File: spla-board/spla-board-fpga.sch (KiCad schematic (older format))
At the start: 4 parts, among them J2 J_JTAG, U1 LFE5U-45F-BG256

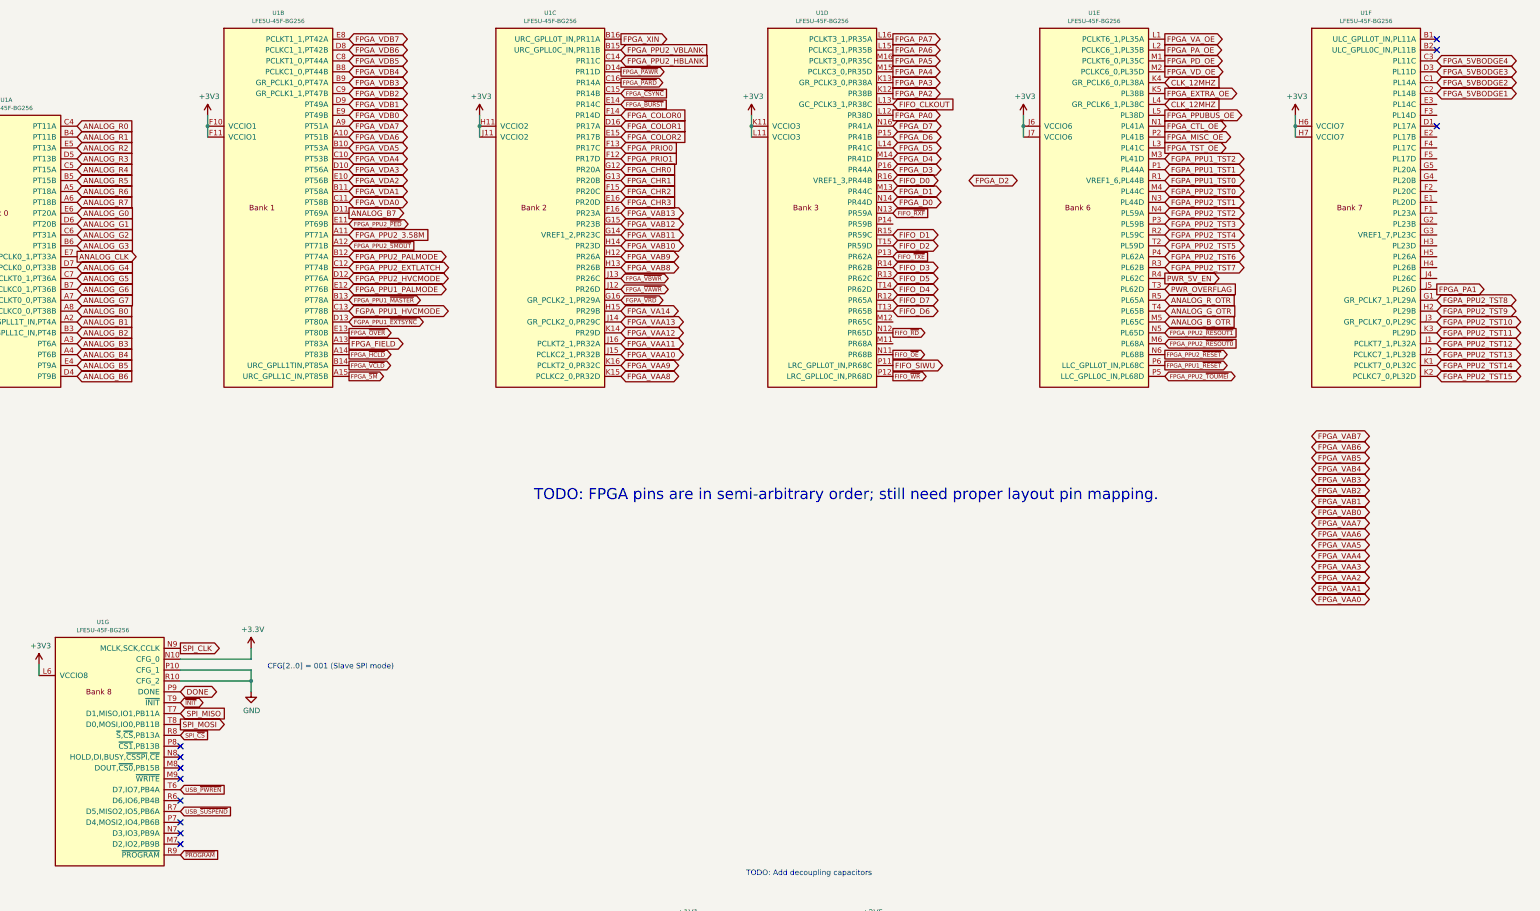
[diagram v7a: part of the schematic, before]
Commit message: schematic: Disconnect FPGA pins temporarily, for pinmapping.
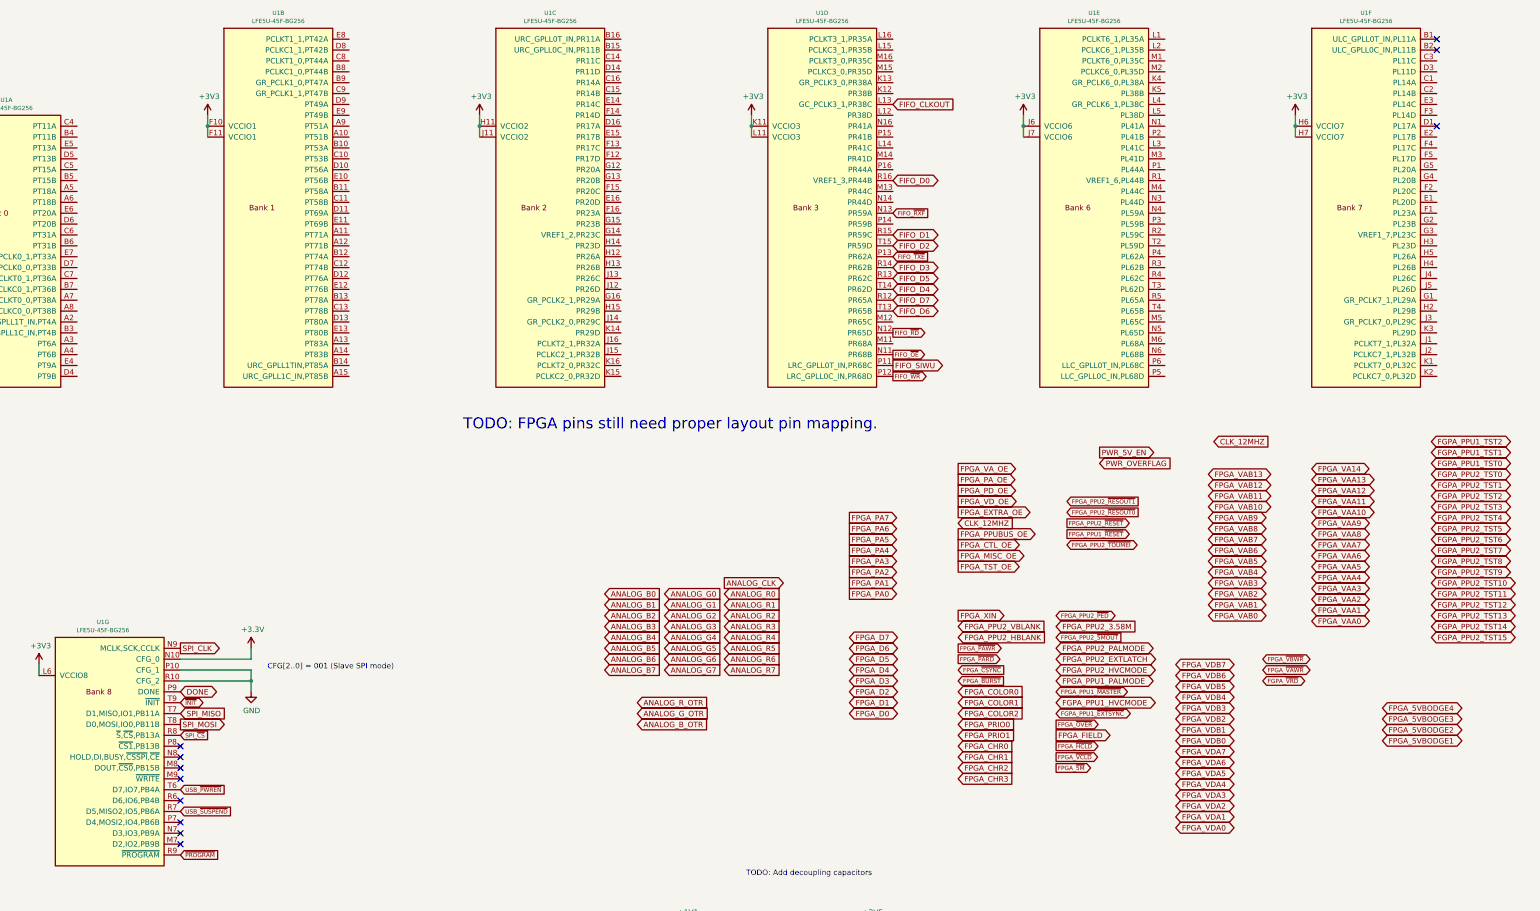
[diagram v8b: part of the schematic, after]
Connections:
- net ANALOG_B0: no longer U1.A8 (PCLKC0_0,PT38B)
- net ANALOG_B1: no longer U1.A2 (ULC_GPLL1T_IN,PT4A)
- net ANALOG_B2: no longer U1.B3 (ULC_GPLL1C_IN,PT4B)
- net ANALOG_B3: no longer U1.A3 (PT6A)
- net ANALOG_B4: no longer U1.A4 (PT6B)
- net ANALOG_B5: no longer U1.E4 (PT9A)
- net ANALOG_B6: no longer U1.D4 (PT9B)
- net ANALOG_B7: no longer U1.D11 (PT69A)
- net ANALOG_B_OTR: no longer U1.M5 (PL65C)
- net ANALOG_CLK: no longer U1.E7 (GR_PCLK0_1,PT33A)
- net ANALOG_G0: no longer U1.E6 (PT20A)
- net ANALOG_G1: no longer U1.D6 (PT20B)
- net ANALOG_G2: no longer U1.C6 (PT31A)
- net ANALOG_G3: no longer U1.B6 (PT31B)
- net ANALOG_G4: no longer U1.D7 (GR_PCLK0_0,PT33B)
- net ANALOG_G5: no longer U1.C7 (PCLKT0_1,PT36A)
- net ANALOG_G6: no longer U1.B7 (PCLKC0_1,PT36B)
- net ANALOG_G7: no longer U1.A7 (PCLKT0_0,PT38A)
- net ANALOG_G_OTR: no longer U1.T4 (PL65B)
- net ANALOG_R0: no longer U1.C4 (PT11A)
- net ANALOG_R1: no longer U1.B4 (PT11B)
- net ANALOG_R2: no longer U1.E5 (PT13A)
- net ANALOG_R3: no longer U1.D5 (PT13B)
- net ANALOG_R4: no longer U1.C5 (PT15A)
- net ANALOG_R5: no longer U1.B5 (PT15B)
- net ANALOG_R6: no longer U1.A5 (PT18A)
- net ANALOG_R7: no longer U1.A6 (PT18B)
- net ANALOG_R_OTR: no longer U1.R5 (PL65A)
- net CLK_12MHZ: no longer U1.K4 (GR_PCLK6_0,PL38A), U1.L4 (GR_PCLK6_1,PL38C)
- net FGPA_PPU1_HVCMODE: no longer U1.C13 (PT78B)
- net FGPA_PPU1_TST0: no longer U1.R1 (VREF1_6,PL44B)
- net FGPA_PPU1_TST1: no longer U1.P1 (PL44A)
- net FGPA_PPU1_TST2: no longer U1.M3 (PL41D)
- net FGPA_PPU1_~EXTSYNC~: no longer U1.D13 (PT80A)
- net FGPA_PPU2_TST0: no longer U1.M4 (PL44C)
- net FGPA_PPU2_TST1: no longer U1.N3 (PL44D)
- net FGPA_PPU2_TST10: no longer U1.J3 (GR_PCLK7_0,PL29C)
- net FGPA_PPU2_TST11: no longer U1.K3 (PL29D)
- net FGPA_PPU2_TST12: no longer U1.J1 (PCLKT7_1,PL32A)
- net FGPA_PPU2_TST13: no longer U1.J2 (PCLKC7_1,PL32B)
- net FGPA_PPU2_TST14: no longer U1.K1 (PCLKT7_0,PL32C)
- net FGPA_PPU2_TST15: no longer U1.K2 (PCLKC7_0,PL32D)
- net FGPA_PPU2_TST2: no longer U1.N4 (PL59A)
- net FGPA_PPU2_TST3: no longer U1.P3 (PL59B)
- net FGPA_PPU2_TST4: no longer U1.R2 (PL59C)
- net FGPA_PPU2_TST5: no longer U1.T2 (PL59D)
- net FGPA_PPU2_TST6: no longer U1.P4 (PL62A)
- net FGPA_PPU2_TST7: no longer U1.R3 (PL62B)
- net FGPA_PPU2_TST8: no longer U1.G1 (GR_PCLK7_1,PL29A)
- net FGPA_PPU2_TST9: no longer U1.H2 (PL29B)
- net FGPA_~VRD~: no longer U1.G16 (GR_PCLK2_1,PR29A)
- net FPGA_5VBODGE1: no longer U1.C2 (PL14B)
- net FPGA_5VBODGE2: no longer U1.C1 (PL14A)
- net FPGA_5VBODGE3: no longer U1.D3 (PL11D)
- net FPGA_5VBODGE4: no longer U1.C3 (PL11C)
- net FPGA_CHR0: no longer U1.G12 (PR20A)
- net FPGA_CHR1: no longer U1.G13 (PR20B)
- net FPGA_CHR2: no longer U1.F15 (PR20C)
- net FPGA_CHR3: no longer U1.E16 (PR20D)
- net FPGA_COLOR0: no longer U1.F14 (PR14D)
- net FPGA_COLOR1: no longer U1.D16 (PR17A)
- net FPGA_COLOR2: no longer U1.E15 (PR17B)
- net FPGA_CTL_OE: no longer U1.N1 (PL41A)
- net FPGA_D0: no longer U1.N14 (PR44D)
- net FPGA_D1: no longer U1.M13 (PR44C)
- net FPGA_D3: no longer U1.P16 (PR44A)
- net FPGA_D4: no longer U1.M14 (PR41D)
- net FPGA_D5: no longer U1.L14 (PR41C)
- net FPGA_D6: no longer U1.P15 (PR41B)
- net FPGA_D7: no longer U1.N16 (PR41A)
- net FPGA_EXTRA_OE: no longer U1.K5 (PL38B)
- net FPGA_FIELD: no longer U1.A13 (PT83A)
- net FPGA_MISC_OE: no longer U1.P2 (PL41B)
- net FPGA_PA0: no longer U1.L12 (PR38D)
- net FPGA_PA1: no longer U1.J5 (PL26D)
- net FPGA_PA2: no longer U1.K12 (PR38B)
- net FPGA_PA3: no longer U1.K13 (GR_PCLK3_0,PR38A)
- net FPGA_PA4: no longer U1.M15 (PCLKC3_0,PR35D)
- net FPGA_PA5: no longer U1.M16 (PCLKT3_0,PR35C)
- net FPGA_PA6: no longer U1.L15 (PCLKC3_1,PR35B)
- net FPGA_PA7: no longer U1.L16 (PCLKT3_1,PR35A)
- net FPGA_PA_OE: no longer U1.L2 (PCLKC6_1,PL35B)
- net FPGA_PD_OE: no longer U1.M1 (PCLKT6_0,PL35C)
- net FPGA_PPU1_PALMODE: no longer U1.E12 (PT76B)
- net FPGA_PPU1_~MASTER~: no longer U1.B13 (PT78A)
- net FPGA_PPU1_~RESET~: no longer U1.P6 (LLC_GPLL0T_IN,PL68C)
- net FPGA_PPU2_3.58M: no longer U1.A11 (PT71A)
- net FPGA_PPU2_EXTLATCH: no longer U1.C12 (PT74B)
- net FPGA_PPU2_HBLANK: no longer U1.C14 (PR11C)
- net FPGA_PPU2_HVCMODE: no longer U1.D12 (PT76A)
- net FPGA_PPU2_PALMODE: no longer U1.B12 (PT74A)
- net FPGA_PPU2_VBLANK: no longer U1.B15 (URC_GPLL0C_IN,PR11B)
- net FPGA_PPU2_~5MOUT~: no longer U1.A12 (PT71B)
- net FPGA_PPU2_~PED~: no longer U1.E11 (PT69B)
- net FPGA_PPU2_~RESET~: no longer U1.N6 (PL68B)
- net FPGA_PPU2_~RESOUT0~: no longer U1.M6 (PL68A)
- net FPGA_PPU2_~RESOUT1~: no longer U1.N5 (PL65D)
- net FPGA_PPU2_~TOUMEI~: no longer U1.P5 (LLC_GPLL0C_IN,PL68D)
- net FPGA_PPUBUS_OE: no longer U1.L5 (PL38D)
- net FPGA_PRIO0: no longer U1.F13 (PR17C)
- net FPGA_PRIO1: no longer U1.F12 (PR17D)
- net FPGA_TST_OE: no longer U1.L3 (PL41C)
- net FPGA_VA14: no longer U1.H15 (PR29B)
- net FPGA_VAA10: no longer U1.J15 (PCLKC2_1,PR32B)
- net FPGA_VAA11: no longer U1.J16 (PCLKT2_1,PR32A)
- net FPGA_VAA12: no longer U1.K14 (PR29D)
- net FPGA_VAA13: no longer U1.J14 (GR_PCLK2_0,PR29C)
- net FPGA_VAA8: no longer U1.K15 (PCLKC2_0,PR32D)
- net FPGA_VAA9: no longer U1.K16 (PCLKT2_0,PR32C)
- net FPGA_VAB10: no longer U1.H14 (PR23D)
- net FPGA_VAB11: no longer U1.G14 (VREF1_2,PR23C)
- net FPGA_VAB12: no longer U1.G15 (PR23B)
- net FPGA_VAB13: no longer U1.F16 (PR23A)
- net FPGA_VAB8: no longer U1.H13 (PR26B)
- net FPGA_VAB9: no longer U1.H12 (PR26A)
- net FPGA_VA_OE: no longer U1.L1 (PCLKT6_1,PL35A)
- net FPGA_VDA0: no longer U1.C11 (PT58B)
- net FPGA_VDA1: no longer U1.B11 (PT58A)
- net FPGA_VDA2: no longer U1.E10 (PT56B)
- net FPGA_VDA3: no longer U1.D10 (PT56A)
- net FPGA_VDA4: no longer U1.C10 (PT53B)
- net FPGA_VDA5: no longer U1.B10 (PT53A)
- net FPGA_VDA6: no longer U1.A10 (PT51B)
- net FPGA_VDA7: no longer U1.A9 (PT51A)
- net FPGA_VDB0: no longer U1.E9 (PT49B)
- net FPGA_VDB1: no longer U1.D9 (PT49A)
- net FPGA_VDB2: no longer U1.C9 (GR_PCLK1_1,PT47B)
- net FPGA_VDB3: no longer U1.B9 (GR_PCLK1_0,PT47A)
- net FPGA_VDB4: no longer U1.B8 (PCLKC1_0,PT44B)
- net FPGA_VDB5: no longer U1.C8 (PCLKT1_0,PT44A)
- net FPGA_VDB6: no longer U1.D8 (PCLKC1_1,PT42B)
- net FPGA_VDB7: no longer U1.E8 (PCLKT1_1,PT42A)
- net FPGA_VD_OE: no longer U1.M2 (PCLKC6_0,PL35D)
- net FPGA_XIN: no longer U1.B16 (URC_GPLL0T_IN,PR11A)
- net FPGA_~5M~: no longer U1.A15 (URC_GPLL1C_IN,PT85B)
- net FPGA_~BURST~: no longer U1.E14 (PR14C)
- net FPGA_~CSYNC~: no longer U1.C15 (PR14B)
- net FPGA_~HCLD: no longer U1.A14 (PT83B)
- net FPGA_~OVER~: no longer U1.E13 (PT80B)
- net FPGA_~PARD~: no longer U1.C16 (PR14A)
- net FPGA_~PAWR~: no longer U1.D14 (PR11D)
- net FPGA_~VAWR~: no longer U1.J12 (PR26D)
- net FPGA_~VBWR~: no longer U1.J13 (PR26C)
- net FPGA_~VCLD~: no longer U1.B14 (URC_GPLL1TIN,PT85A)
- net PWR_5V_EN: no longer U1.R4 (PL62C)
- net PWR_OVERFLAG: no longer U1.T3 (PL62D)
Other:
- note added: "TODO: FPGA pins still need proper layout pin mapping."
- note removed: "TODO: FPGA pins are in semi-arbitrary order; still need proper layout pin mapping."
